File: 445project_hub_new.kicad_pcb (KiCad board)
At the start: 2 copper layers, 100 x 100 mm, 106 parts, among them J101 Barrel_Jack_Switch, J102 USB_B, J104 USB, J201 Conn_01x04, J202 Conn_01x04, J203 Conn_02x05_Odd_Even, J204 Conn_02x05_Odd_Even, J205 Conn_01x04, J206 Conn_02x05_Odd_Even, J301 Conn_02x06_Odd_Even, J302 Conn_01x10, J303 Conn_01x04, SW101 SW_Push, U101 MCP1826S, U102 SN75240, U103 TUSB2046I, U105 SN75240, U201 MCP2221AxSL, U202 MCP2221AxSL, U203 MCP2221AxSL, U301 MCP7940N-xSN, U302 MCP23017_SO, U303 DS2482-100, Y101 6MHz, Y301 Crystal

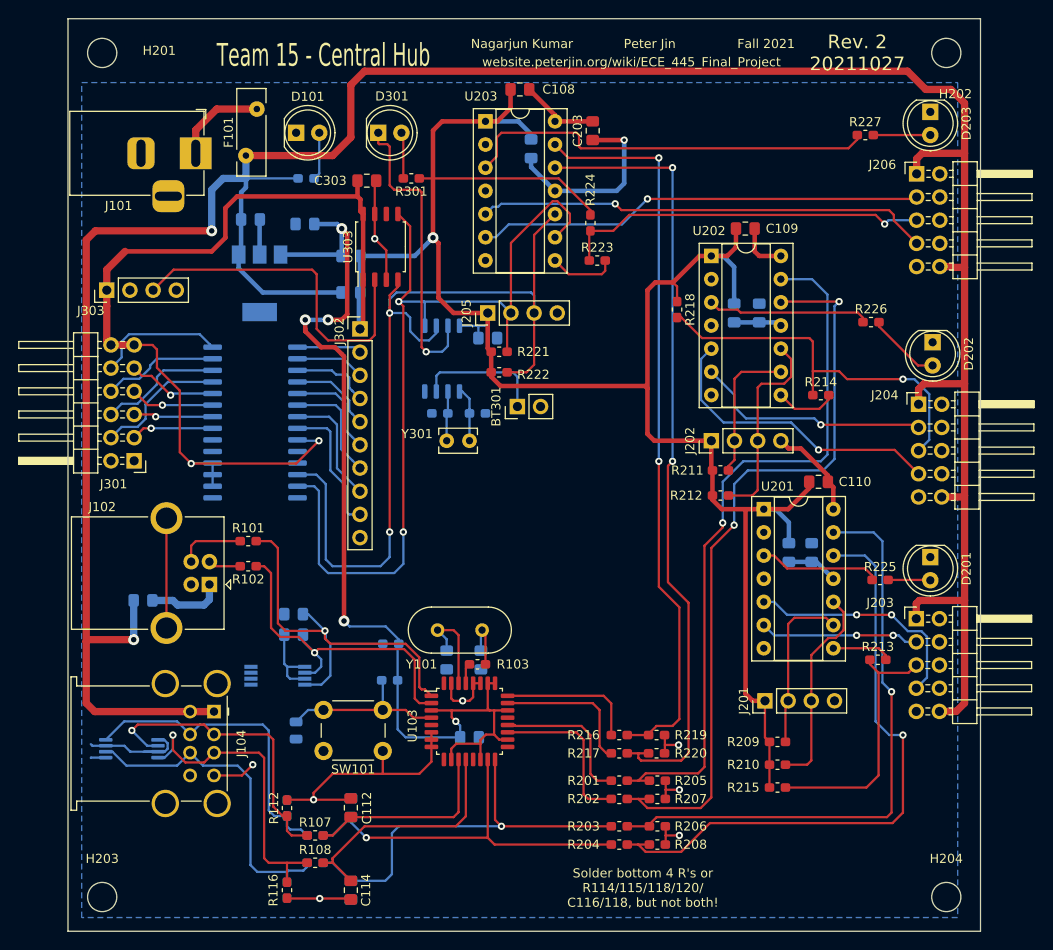
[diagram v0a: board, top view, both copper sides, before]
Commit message: Add capacitors on central hub
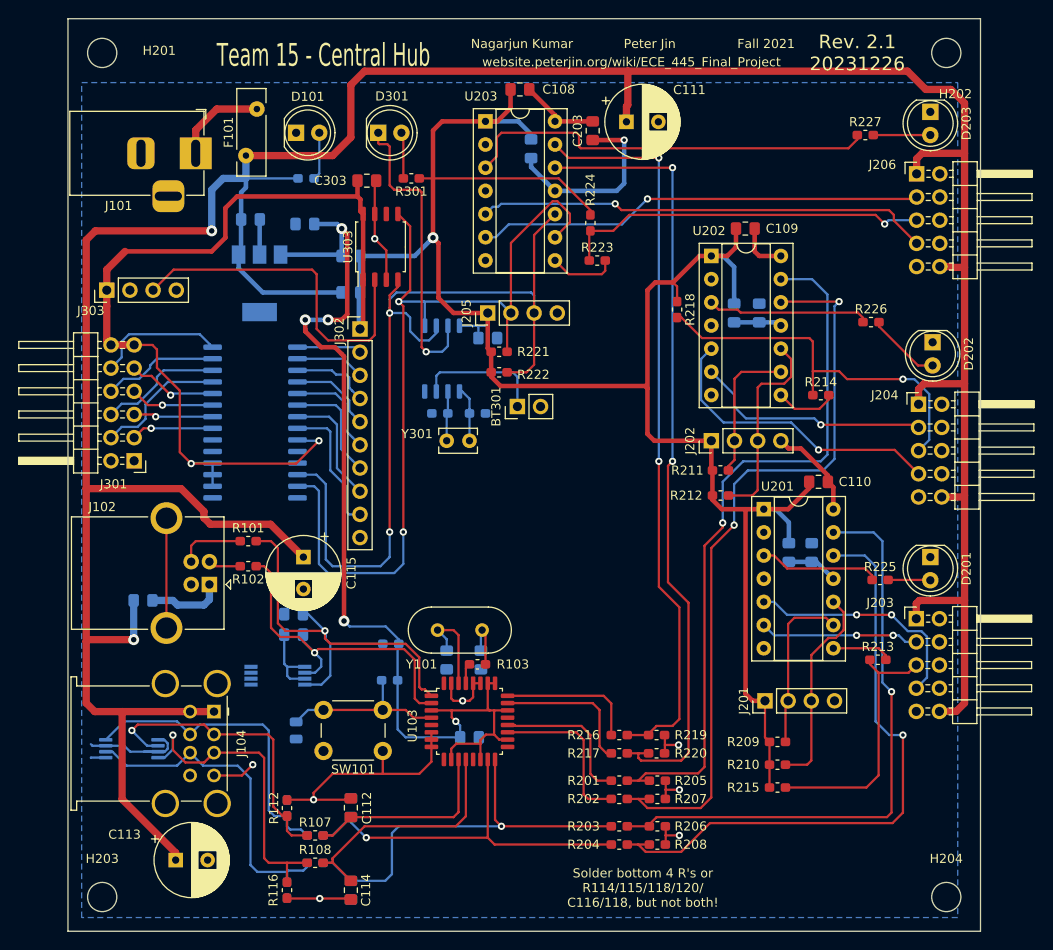
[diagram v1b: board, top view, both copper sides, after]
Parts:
- added C111: C_Polarized, Capacitor_THT:CP_Radial_D8.0mm_P3.50mm, F.Cu at (131.2, 51.3)
- added C113: C_Polarized, Capacitor_THT:CP_Radial_D8.0mm_P3.50mm, F.Cu at (81.8, 132.2)
- added C115: C_Polarized, Capacitor_THT:CP_Radial_D8.0mm_P3.50mm, F.Cu at (95.8, 99.0)
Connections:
- J101 pad 3: Net-(J101-Pad3) -> unconnected-(J101-Pad3)
- J102 pad 5: Net-(J102-Pad5) -> unconnected-(J102-Pad5)
- J203 pad 4: Net-(J203-Pad4) -> unconnected-(J203-Pad4)
- J203 pad 8: Net-(J203-Pad8) -> unconnected-(J203-Pad8)
- J204 pad 4: Net-(J204-Pad4) -> unconnected-(J204-Pad4)
- J204 pad 8: Net-(J204-Pad8) -> unconnected-(J204-Pad8)
- J206 pad 4: Net-(J206-Pad4) -> unconnected-(J206-Pad4)
- J206 pad 8: Net-(J206-Pad8) -> unconnected-(J206-Pad8)
- J303 pad 2: Net-(J303-Pad2) -> unconnected-(J303-Pad2)
- U103 pad 13: Net-(U103-Pad13) -> unconnected-(U103-Pad13)
- U103 pad 17: Net-(U103-Pad17) -> unconnected-(U103-Pad17)
- U103 pad 21: Net-(U103-Pad21) -> unconnected-(U103-Pad21)
- U103 pad 32: Net-(U103-Pad32) -> unconnected-(U103-Pad32)
- U103 pad 5: Net-(U103-Pad5) -> unconnected-(U103-Pad5)
- U103 pad 9: Net-(U103-Pad9) -> unconnected-(U103-Pad9)
- U201 pad 2: Net-(U201-Pad2) -> unconnected-(U201-Pad2)
- U201 pad 4: Net-(U201-Pad4) -> unconnected-(U201-Pad4)
- U201 pad 7: Net-(U201-Pad7) -> unconnected-(U201-Pad7)
- U202 pad 2: Net-(U202-Pad2) -> unconnected-(U202-Pad2)
- U202 pad 4: Net-(U202-Pad4) -> unconnected-(U202-Pad4)
- U202 pad 7: Net-(U202-Pad7) -> unconnected-(U202-Pad7)
- U203 pad 2: Net-(U203-Pad2) -> unconnected-(U203-Pad2)
- U203 pad 4: Net-(U203-Pad4) -> unconnected-(U203-Pad4)
- U203 pad 7: Net-(U203-Pad7) -> unconnected-(U203-Pad7)
- U302 pad 11: Net-(U302-Pad11) -> unconnected-(U302-Pad11)
- U302 pad 14: Net-(U302-Pad14) -> unconnected-(U302-Pad14)
- U302 pad 19: Net-(U302-Pad19) -> unconnected-(U302-Pad19)
- U302 pad 20: Net-(U302-Pad20) -> unconnected-(U302-Pad20)
- U303 pad 6: Net-(U303-Pad6) -> unconnected-(U303-Pad6)
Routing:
- net +5V: track 311.4 -> 363.0 mm
- net unconnected-(J102-Pad5): track 0.00 -> 12.0 mm
- net Net-(J102-Pad5): track 12.0 -> 0.00 mm
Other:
- net class Default removed
- board text added: "Rev. 2.1 20231226"
- board text added: "Solder this part or -> R203/204/206/208, but not both!"
- board text removed: "<- Solder this part or R203/204/206/208, but not both!"
- board text removed: "Rev. 2 20211027"

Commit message: New Central Hub: Add USB-C, 5V->3.3V regulator
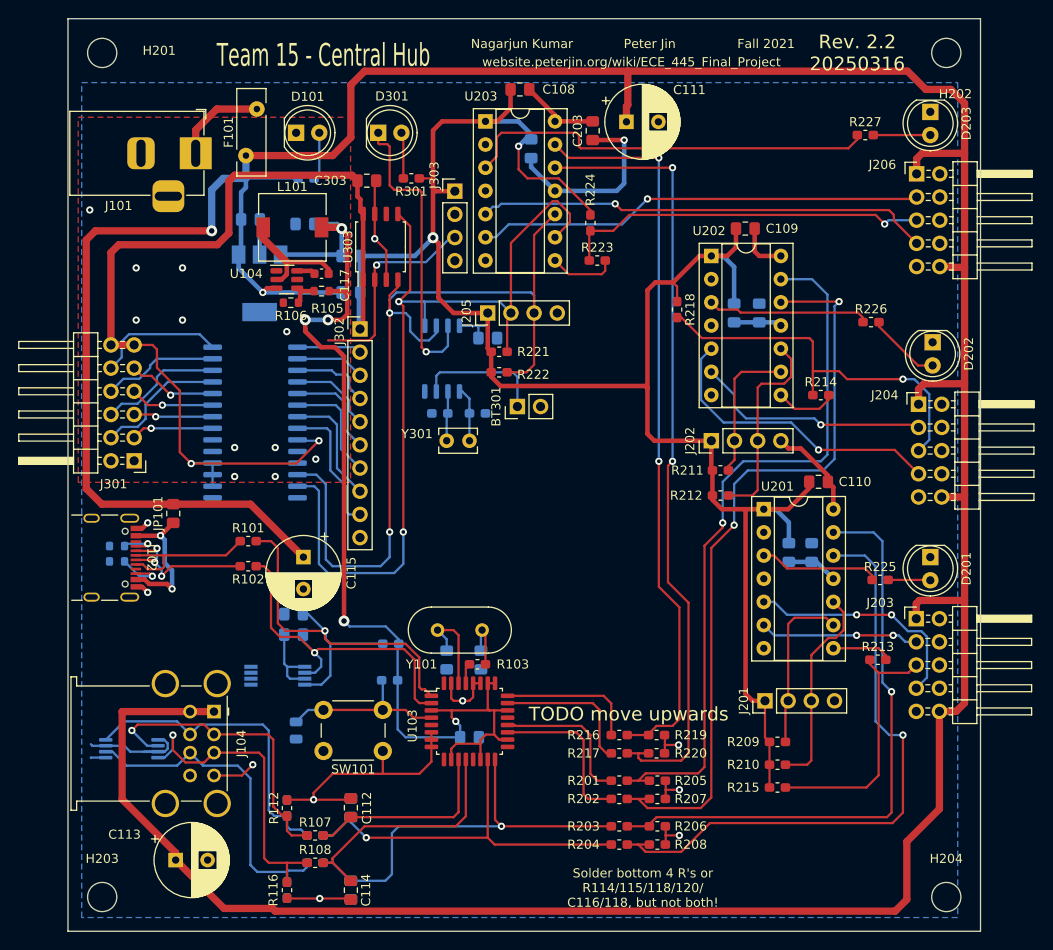
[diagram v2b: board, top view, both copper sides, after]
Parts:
- added C117: C, Capacitor_SMD:C_0603_1608Metric, F.Cu at (97.8, 67.9)
- added L101: L, Inductor_SMD:L_7.3x7.3_H3.5, F.Cu at (94.6, 62.9)
- added R105: R, Resistor_SMD:R_0603_1608Metric, F.Cu at (97.8, 69.8)
- added R106: R, Resistor_SMD:R_0603_1608Metric, F.Cu at (94.4, 71.1)
- added R109: R, Resistor_SMD:R_0603_1608Metric, B.Cu at (75.4, 97.8)
- added R110: R, Resistor_SMD:R_0603_1608Metric, B.Cu at (75.4, 99.5)
- added U104: TPS54302, Package_TO_SOT_SMD:SOT-23-6, F.Cu at (94.0, 68.6)
- J102: value USB_B -> USB_C_Receptacle_USB2.0; footprint Connector_USB:USB_B_OST_USB-B1HSxx_Horizontal -> Library:USB_C_Receptacle_GCT_USB4105-xx-A_16P_TopMnt_Horizontal
- JP101: moved to F.Cu
- moved J303 39.7 mm to (112.4, 58.9), turned to 0 degrees
- moved J102 12.2 mm to (73.7, 99.1), turned to -90 degrees
- moved JP101 10.1 mm to (81.5, 94.2), turned to 90 degrees
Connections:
- JP101 pad 1: Net-(J102-Pad1) -> Net-(J102-PadA4)
- R101 pad 1: Net-(J102-Pad3) -> Net-(J102-PadA6)
- R102 pad 2: Net-(J102-Pad2) -> Net-(J102-PadA7)
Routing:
- net +5V: track 363.0 -> 432.0 mm
- net Net-(J102-PadA7): track 0.00 -> 17.1 mm, vias 0 -> 3
- net Net-(J102-PadA6): track 0.00 -> 16.7 mm
- net Net-(J102-PadA4): track 0.00 -> 15.4 mm, vias 0 -> 2
- net Net-(J303-Pad3): track 38.3 -> 22.9 mm, vias 0 -> 1
- net Net-(C117-Pad2): track 0.00 -> 13.0 mm
- net unconnected-(J102-Pad5): track 12.0 -> 0.00 mm
- net Net-(J102-Pad1): track 8.36 -> 0.00 mm
- net Net-(J102-Pad3): track 7.33 -> 0.00 mm
- net Net-(J102-PadB5): track 0.00 -> 5.64 mm, vias 0 -> 1
- net +3V3: track 115.4 -> 119.8 mm
- net Net-(J102-PadA5): track 0.00 -> 4.06 mm, vias 0 -> 1
- net Net-(J102-Pad2): track 3.58 -> 0.00 mm
- net Net-(R105-Pad2): track 0.00 -> 3.33 mm
- net GND: track 120.4 -> 123.5 mm, vias 8 -> 21
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- added copper zone on F.Cu, net GND
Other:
- board text added: "Rev. 2.2 20250316"
- board text added: "TODO move upwards"
- board text removed: "Rev. 2.1 20231226"
